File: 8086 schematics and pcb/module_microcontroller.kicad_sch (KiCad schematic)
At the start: 1 part, among them U2 ATmega328P-A

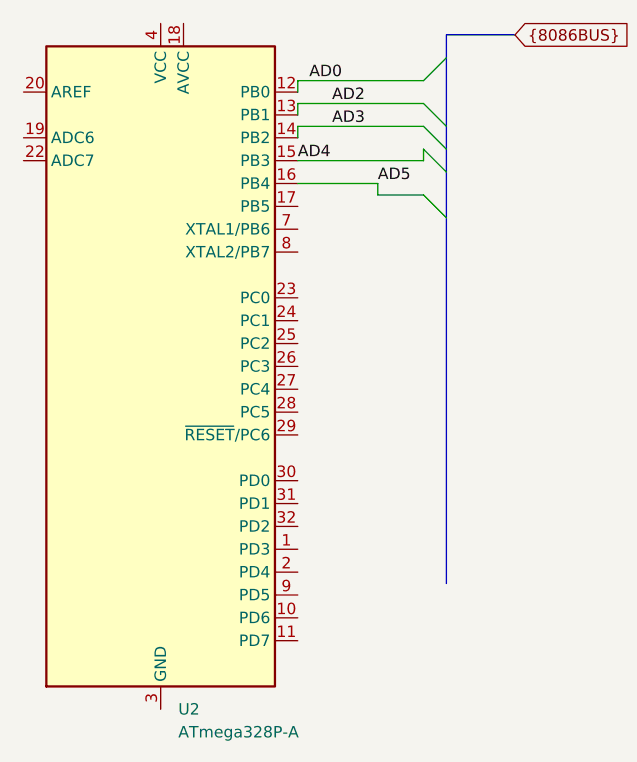
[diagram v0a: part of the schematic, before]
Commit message: 8086 module - bus connected
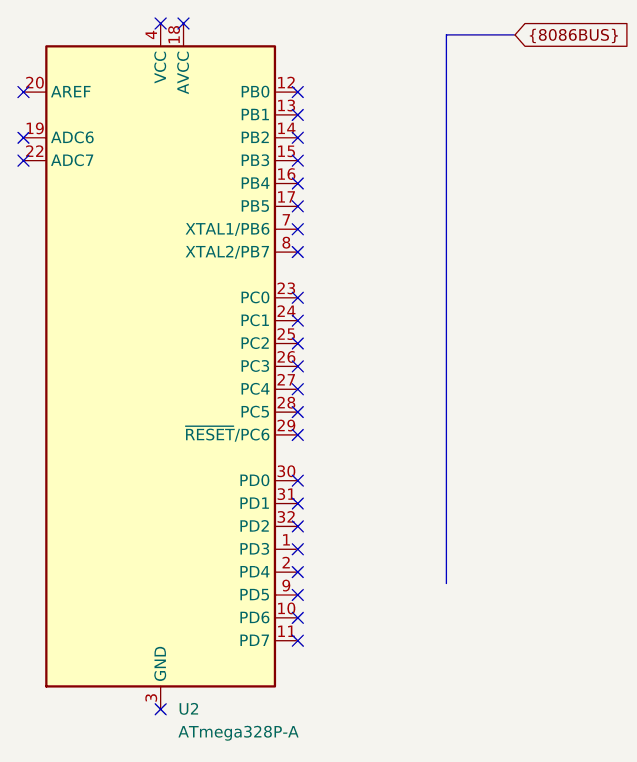
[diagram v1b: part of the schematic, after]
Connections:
- net AD0: no longer names the net of U2.12 (PB0)
- net AD2: no longer names the net of U2.13 (PB1)
- net AD3: no longer names the net of U2.14 (PB2)
- net AD4: no longer names the net of U2.15 (PB3)
- net AD5: no longer names the net of U2.16 (PB4)
- no-connect marks 0 -> 29
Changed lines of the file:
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@@
 (kicad_sch (version 20230121) (generator eeschema)
   (paper "A4")
-  (bus_entry (at 152.4 73.66) (size -2.54 -2.54)
-    (stroke (width 0) (type default))
-  )
-  (bus_entry (at 152.4 78.74) (size -2.54 -2.54)
-    (stroke (width 0) (type default))
-  )
-  (bus_entry (at 152.4 66.04) (size -2.54 2.54)
-    (stroke (width 0) (type default))
-  )
-  (bus_entry (at 152.4 76.2) (size -2.54 -2.54)
-    (stroke (width 0) (type default))
-  )
-  (bus_entry (at 152.4 83.82) (size -2.54 -2.54)
-    (stroke (width 0) (type default))
-  )
-  (bus (pts (xy 152.4 83.82) (xy 152.4 124.46))
-    (stroke (width 0) (type default))
-  )
-  (wire (pts (xy 149.86 71.12) (xy 135.89 71.12))
-    (stroke (width 0) (type default))
-  )
-  (wire (pts (xy 135.89 73.66) (xy 135.89 74.93))
-    (stroke (width 0) (type default))
-  )
-  (wire (pts (xy 135.89 71.12) (xy 135.89 72.39))
-    (stroke (width 0) (type default))
-  )
-  (wire (pts (xy 135.89 80.01) (xy 144.78 80.01))
-    (stroke (width 0) (type default))
-  )
-  (wire (pts (xy 149.86 76.2) (xy 149.86 77.47))
-    (stroke (width 0) (type default))
-  )
-  (wire (pts (xy 135.89 68.58) (xy 149.86 68.58))
-    (stroke (width 0) (type default))
-  )
-  (wire (pts (xy 149.86 77.47) (xy 135.89 77.47))
-    (stroke (width 0) (type default))
-  )
-  (bus (pts (xy 152.4 73.66) (xy 152.4 76.2))
-    (stroke (width 0) (type default))
-  )
-  (bus (pts (xy 152.4 66.04) (xy 152.4 73.66))
-    (stroke (width 0) (type default))
-  )
-  (wire (pts (xy 144.78 81.28) (xy 144.78 80.01))
-    (stroke (width 0) (type default))
-  )
-  (wire (pts (xy 149.86 73.66) (xy 135.89 73.66))
-    (stroke (width 0) (type default))
-  )
-  (bus (pts (xy 152.4 78.74) (xy 152.4 83.82))
-    (stroke (width 0) (type default))
-  )
-  (bus (pts (xy 152.4 63.5) (xy 152.4 66.04))
-    (stroke (width 0) (type default))
-  )
-  (bus (pts (xy 152.4 76.2) (xy 152.4 78.74))
+  (no_connect (at 135.89 105.41))
+  (no_connect (at 135.89 102.87))
+  (no_connect (at 135.89 125.73))
+  (no_connect (at 135.89 97.79))
+  (no_connect (at 135.89 118.11))
+  (no_connect (at 135.89 77.47))
+  (no_connect (at 135.89 82.55))
+  (no_connect (at 123.19 62.23))
+  (no_connect (at 120.65 138.43))
+  (no_connect (at 135.89 100.33))
+  (no_connect (at 135.89 92.71))
+  (no_connect (at 105.41 77.47))
+  (no_connect (at 135.89 115.57))
+  (no_connect (at 105.41 74.93))
+  (no_connect (at 135.89 113.03))
+  (no_connect (at 135.89 130.81))
+  (no_connect (at 135.89 72.39))
+  (no_connect (at 135.89 123.19))
+  (no_connect (at 105.41 69.85))
+  (no_connect (at 135.89 120.65))
+  (no_connect (at 135.89 80.01))
+  (no_connect (at 135.89 107.95))
+  (no_connect (at 135.89 128.27))
+  (no_connect (at 135.89 87.63))
+  (no_connect (at 135.89 85.09))
+  (no_connect (at 135.89 95.25))
+  (no_connect (at 120.65 62.23))
+  (no_connect (at 135.89 69.85))
+  (no_connect (at 135.89 74.93))
+  (bus (pts (xy 152.4 63.5) (xy 152.4 124.46))
     (stroke (width 0) (type default))
   )
@@
     (stroke (width 0) (type default))
   )
-  (wire (pts (xy 149.86 81.28) (xy 144.78 81.28))
-    (stroke (width 0) (type default))
-  )
-  (wire (pts (xy 135.89 68.58) (xy 135.89 69.85))
-    (stroke (width 0) (type default))
-  )
-  (label "AD2" (at 139.7 71.12 0)
-    (effects (font (size 1.27 1.27)) (justify left bottom))
-  )
-  (label "AD0" (at 137.16 68.58 0)
-    (effects (font (size 1.27 1.27)) (justify left bottom))
-  )
-  (label "AD5" (at 144.78 80.01 0)
-    (effects (font (size 1.27 1.27)) (justify left bottom))
-  )
-  (label "AD3" (at 139.7 73.66 0)
-    (effects (font (size 1.27 1.27)) (justify left bottom))
-  )
-  (label "AD4" (at 135.89 77.47 0)
-    (effects (font (size 1.27 1.27)) (justify left bottom))
-  )
   (global_label "{8086BUS}" (shape input) (at 160.02 63.5 0) (fields_autoplaced)

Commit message: basic start for microcontroller module
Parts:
- added U10, U11, U12: 74HC595, symbol 74xx:74HC595
- added U13, U14: 74HC165, symbol 8086PC:74HC165
- added U25: CP2102N-Axx-xQFN28, Package_DFN_QFN:QFN-28-1EP_5x5mm_P0.5mm_EP3.35x3.35mm, symbol Interface_USB:CP2102N-Axx-xQFN28
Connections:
- net ~{WR}: now reaches U2.1 (PD3)
- net RESET: now reaches U2.10 (PD6)
- net ~{INTA}: now reaches U2.11 (PD7)
- net HOLD: now reaches U2.12 (PB0)
- net HLDA: now reaches U2.13 (PB1)
- net REG_RCLK: now reaches U2.14 (PB2)
- net REG_RCLK: now also U10.12 (RCLK), U11.12 (RCLK), U12.12 (RCLK)
- net SPI_MOSI: now reaches U2.15 (PB3)
- net SPI_MOSI: now also U10.14 (SER)
- net SPI_MISO: now reaches U2.16 (PB4)
- net SPI_MISO: now also U14.9 (QH)
- net SPI_SCK: now reaches U2.17 (PB5)
- net SPI_SCK: now also U10.11 (SRCLK), U11.11 (SRCLK), U12.11 (SRCLK)
- net +5V: now reaches U2.18 (AVCC)
- net +5V: now also U2.4 (VCC), U2.6 (VCC), U10.16 (VCC), U11.16 (VCC), U12.16 (VCC), U13.16 (V_{CC}), U14.16 (V_{CC})
- net BUSALE: now reaches U2.2 (PD4)
- net GND: now reaches U2.21 (GND), U2.3 (GND), U2.5 (GND)
- net GND: now also U10.10 (~{SRCLR}), U10.8 (GND), U11.10 (~{SRCLR}), U11.8 (GND), U12.10 (~{SRCLR}), U12.8 (GND), U13.8 (GND), U14.8 (GND)
- net REG_OE: now reaches U2.23 (PC0)
- net REG_OE: now also U10.13 (~{OE}), U11.13 (~{OE}), U12.13 (~{OE})
- net REG_SHLD: now reaches U2.24 (PC1)
- net REG_SHLD: now also U13.1 (SH/~{LD}), U14.1 (SH/~{LD})
- net INTR: now reaches U2.25 (PC2)
- net NMI: now reaches U2.26 (PC3)
- net ~{TEST}: now reaches U2.27 (PC4)
- net READY: now reaches U2.28 (PC5)
- net ~{RD}: now reaches U2.32 (PD2)
- net CLK: now reaches U2.9 (PD5)
- new net: U10.9 (QH'), U11.14 (SER)
- new net: U11.9 (QH'), U12.14 (SER)
- new net: U25.29 (GND), U25.3 (GND)
- new net A16: U12.15 (QA)
- new net A17: U12.1 (QB)
- new net A18: U12.2 (QC)
- new net A19: U12.3 (QD)
- new net AD0: U10.15 (QA), U13.11 (A)
- new net AD1: U10.1 (QB), U13.12 (B)
- new net AD10: U11.2 (QC), U14.13 (C)
- new net AD11: U11.3 (QD), U14.14 (D)
- new net AD12: U11.4 (QE), U14.3 (E)
- new net AD13: U11.5 (QF), U14.4 (F)
- new net AD14: U11.6 (QG), U14.5 (G)
- new net AD15: U11.7 (QH), U14.6 (H)
- new net AD2: U10.2 (QC), U13.13 (C)
- new net AD3: U10.3 (QD), U13.14 (D)
- new net AD4: U10.4 (QE), U13.3 (E)
- new net AD5: U10.5 (QF), U13.4 (F)
- new net AD6: U10.6 (QG), U13.5 (G)
- new net AD7: U10.7 (QH), U13.6 (H)
- new net AD8: U11.15 (QA), U14.11 (A)
- new net AD9: U11.1 (QB), U14.12 (B)
- no-connect marks 29 -> 49
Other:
- moved on the sheet: U2

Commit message: initial PCB layout with almost accurate footprints
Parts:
- U10, U11, U12, U13, U14: footprint (none) -> Package_SO:SOIC-16W_7.5x10.3mm_P1.27mm
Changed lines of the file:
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@@
       (effects (font (size 1.27 1.27)))
     )
-    (property "Footprint" "" (at 121.92 93.98 0)
+    (property "Footprint" "Package_SO:SOIC-16W_7.5x10.3mm_P1.27mm" (at 121.92 93.98 0)
       (effects (font (size 1.27 1.27)) hide)
     )
@@
       (effects (font (size 1.27 1.27)))
     )
-    (property "Footprint" "" (at 121.92 50.8 0)
+    (property "Footprint" "Package_SO:SOIC-16W_7.5x10.3mm_P1.27mm" (at 121.92 50.8 0)
       (effects (font (size 1.27 1.27)) hide)
     )
@@
       (effects (font (size 1.27 1.27)))
     )
-    (property "Footprint" "" (at 170.18 63.5 0)
+    (property "Footprint" "Package_SO:SOIC-16W_7.5x10.3mm_P1.27mm" (at 170.18 63.5 0)
       (effects (font (size 1.27 1.27)) hide)
     )
@@
       (effects (font (size 1.27 1.27)))
     )
-    (property "Footprint" "" (at 170.18 124.46 0)
+    (property "Footprint" "Package_SO:SOIC-16W_7.5x10.3mm_P1.27mm" (at 170.18 124.46 0)
       (effects (font (size 1.27 1.27)) hide)
     )
@@
       (effects (font (size 1.27 1.27)))
     )
-    (property "Footprint" "" (at 121.92 137.16 0)
-      (effects (font (size 1.27 1.27)) hide)
-    )
+    (property "Footprint" "Package_SO:SOIC-16W_7.5x10.3mm_P1.27mm" (at 121.92 137.16 0)
+      (effects (font (size 1.27 1.27)) hide)
+    )
